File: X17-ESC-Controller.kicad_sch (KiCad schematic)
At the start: 8 parts, among them IC1 STM32F091CCT7, J2 DF11-10DP-2DSA24, J3 DF11-10DP-2DSA24, U1 AZ1117H-ADJ, U2 MAX485CSA+T

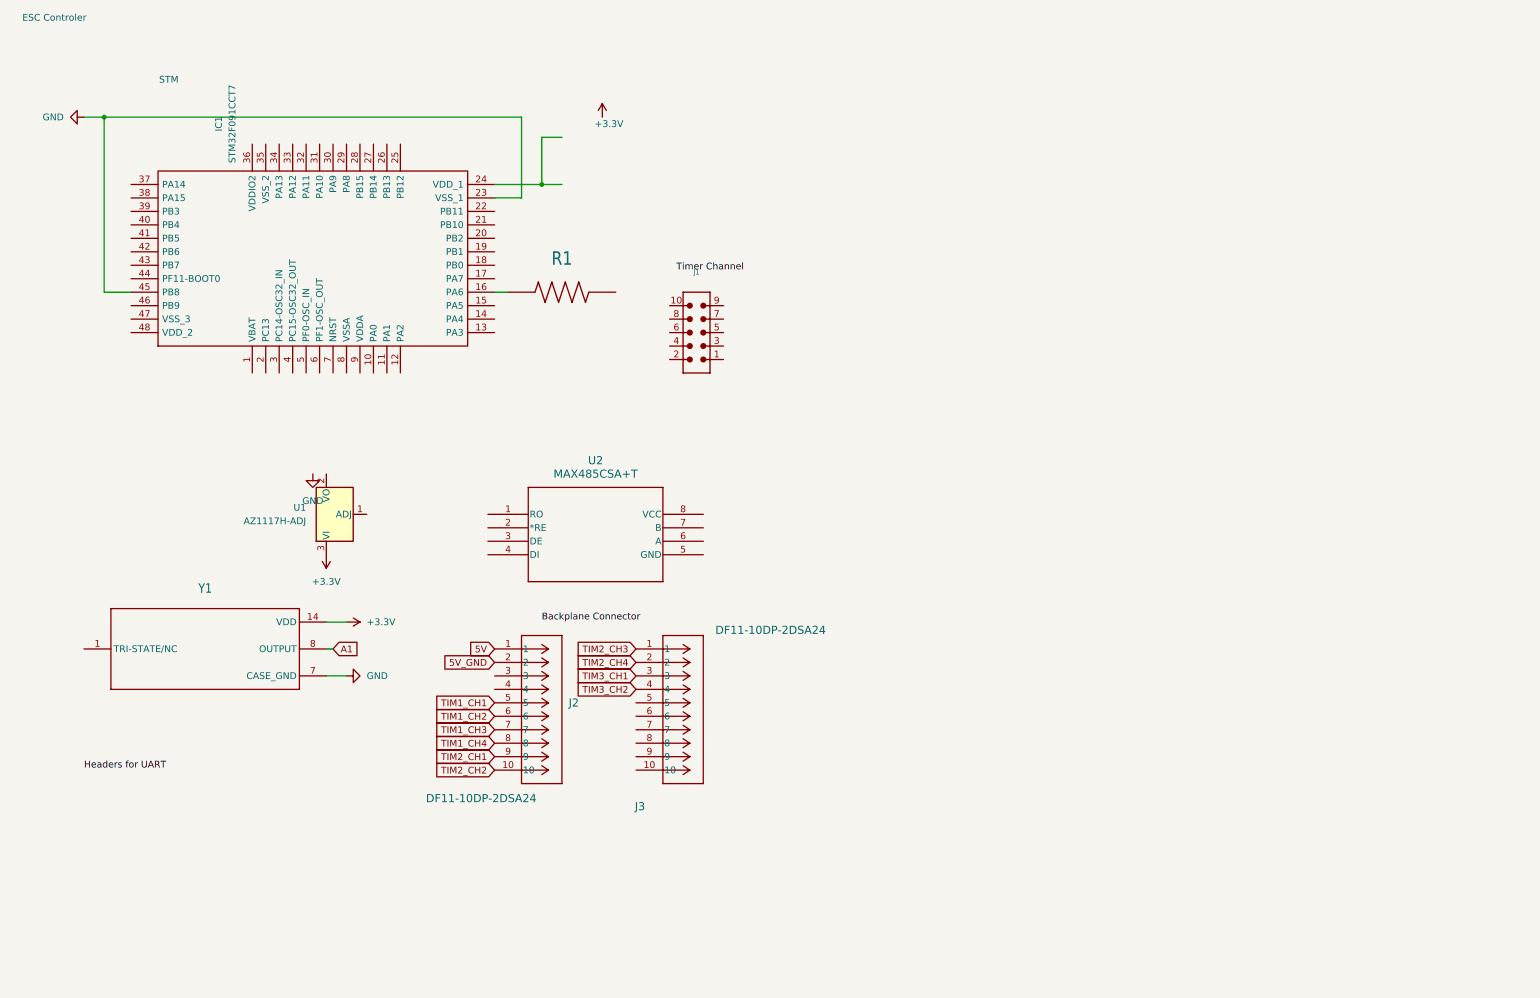
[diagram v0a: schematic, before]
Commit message: X17 ESC Controller Schematic
New updated schematic
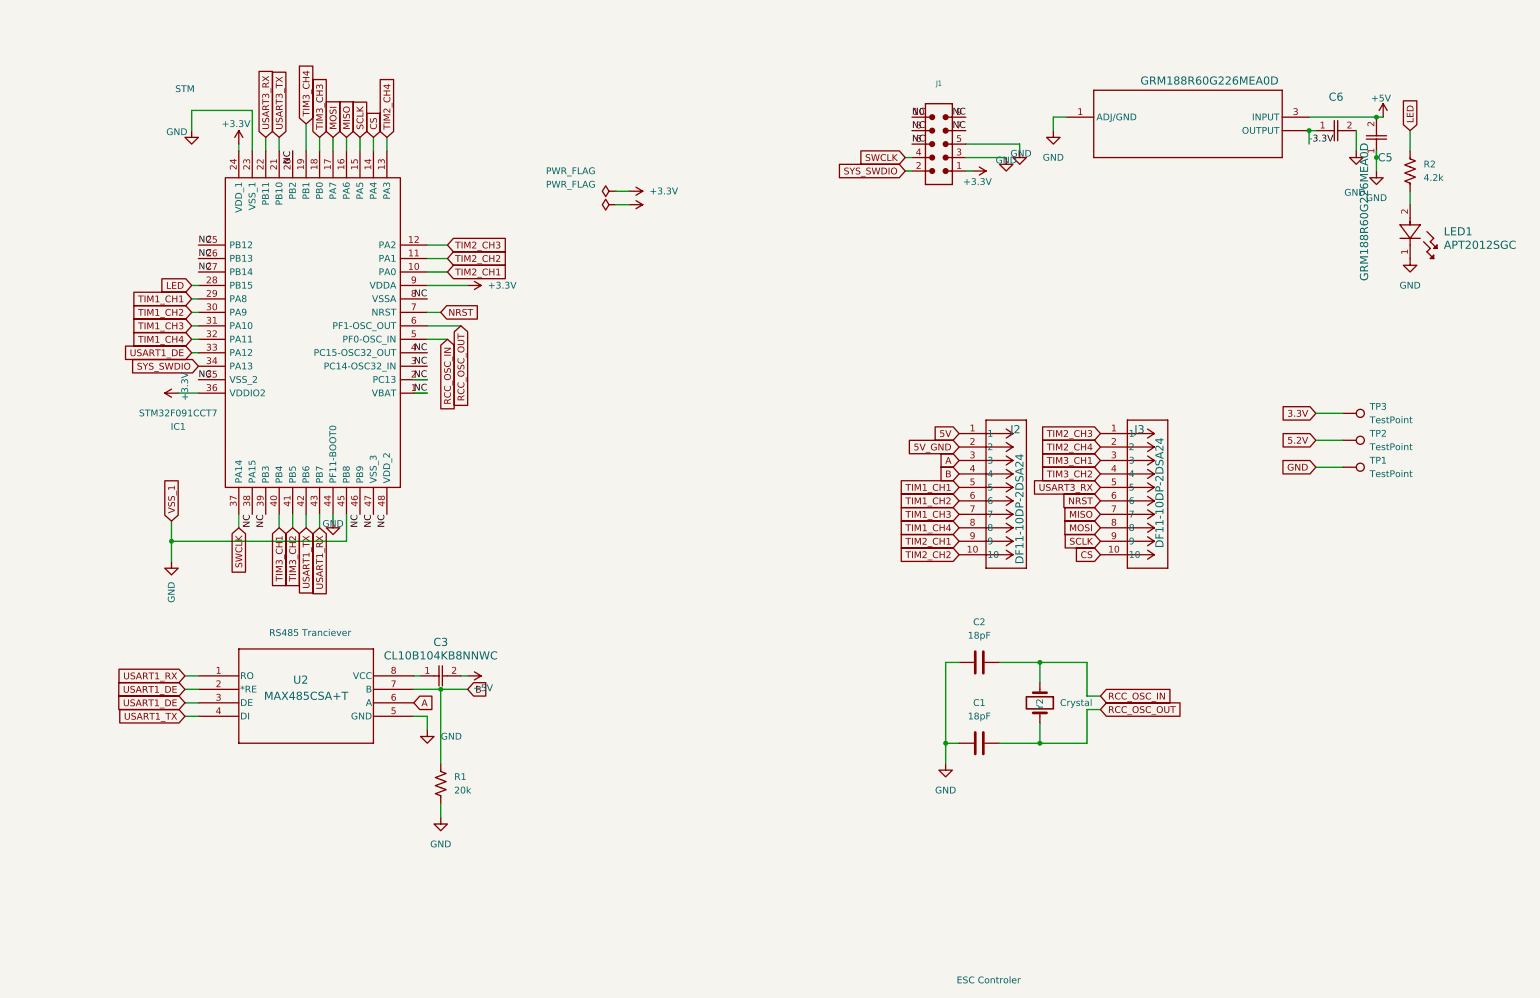
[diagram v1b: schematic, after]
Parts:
- removed R1: ~, CRGCQ0603F1K0:RESC1608X55N, symbol CRGCQ0603F1K0:CRGCQ0603F1K0
- removed U1: AZ1117H-ADJ, Package_TO_SOT_SMD:SOT-223-3_TabPin2, symbol Regulator_Linear:AZ1117H-ADJ
- removed Y1: ~, ACO-8.000MHZ-EK:XTAL_ACO-8.000MHZ-EK, symbol ACO-8.000MHZ-EK:ACO-8.000MHZ-EK
- added C1, C2: 18pF, symbol Device:C
- added C3: CL10B104KB8NNWC, CAP_CL10_SAM, symbol 2024-10-16_23-50-01:CL10B104KB8NNWC
- added C5, C6: GRM188R60G226MEA0D, G-188_MUR, symbol 2024-10-30_23-26-29:GRM188R60G226MEA0D
- added LED1: APT2012SGC, LED_APT2012SGC_KNB, symbol 2024-10-19_19-01-08:APT2012SGC
- added R1: 20k, symbol Device:R_US
- added R2: 4.2k, symbol Device:R_US
- added TP1, TP2, TP3: TestPoint, symbol Connector:TestPoint
- added U3: ~, X16-ESC-Controller:SOT223_AZ1117I_6P5X3P5_DIO, symbol X16-ESC-Controller:AZ1117IH-3.3TRG1
- added Y2: Crystal, symbol Device:Crystal
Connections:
- net +3.3V: now also IC1.24 (VDD_1), IC1.36 (VDDIO2), IC1.9 (VDDA), J1.1
- net GND: now also IC1.44 (PF11-BOOT0), J1.3, J1.5, U2.5 (GND), C1.2, C2.2, C5.1, C6.2, LED1.1, R1.2, TP1.1, U3.1 (ADJ/GND)
- net TIM1_CH1: now also IC1.29 (PA8)
- net TIM1_CH2: now also IC1.30 (PA9)
- net TIM1_CH3: now also IC1.31 (PA10)
- net TIM1_CH4: now also IC1.32 (PA11)
- net TIM2_CH1: now also IC1.10 (PA0)
- net TIM2_CH2: now also IC1.11 (PA1)
- net TIM2_CH3: now also IC1.12 (PA2)
- net TIM2_CH4: now also IC1.13 (PA3)
- net TIM3_CH1: now also IC1.40 (PB4)
- net TIM3_CH2: now also IC1.41 (PB5)
- net MISO: now reaches IC1.16 (PA6)
- net MISO: now also J3.7
- net A: now reaches J2.3
- net A: now also U2.6 (A)
- net B: now reaches J2.4
- net B: now also U2.7 (B), R1.1
- net USART1_RX: now reaches U2.1 (RO)
- net USART1_RX: now also IC1.43 (PB7)
- net USART1_DE: now reaches U2.2 (*RE)
- net USART1_DE: now also IC1.33 (PA12), U2.3 (DE)
- net USART1_TX: now reaches U2.4 (DI)
- net USART1_TX: now also IC1.42 (PB6)
- net at U2.8 (VCC): now also C3.1
- net NC: now reaches IC1.1 (VBAT)
- net NC: now also IC1.2 (PC13), IC1.20 (PB2), IC1.25 (PB12), IC1.26 (PB13), IC1.27 (PB14), IC1.3 (PC14-OSC32_IN), IC1.35 (VSS_2), IC1.38 (PA15), IC1.39 (PB3), IC1.4 (PC15-OSC32_OUT), IC1.46 (PB9), IC1.47 (VSS_3), IC1.48 (VDD_2), IC1.8 (VSSA), J1.10, J1.6, J1.7, J1.8, J1.9
- net CS: now reaches IC1.14 (PA4)
- net CS: now also J3.10
- net SCLK: now reaches IC1.15 (PA5)
- net SCLK: now also J3.9
- net MOSI: now reaches IC1.17 (PA7)
- net MOSI: now also J3.8
- net TIM3_CH3: now reaches IC1.18 (PB0)
- net TIM3_CH4: now reaches IC1.19 (PB1)
- net USART3_TX: now reaches IC1.21 (PB10)
- net USART3_RX: now reaches IC1.22 (PB11)
- net USART3_RX: now also J3.5
- net LED: now reaches IC1.28 (PB15)
- net LED: now also R2.1
- net SYS_SWDIO: now reaches IC1.34 (PA13)
- net SYS_SWDIO: now also J1.2
- net SWCLK: now reaches IC1.37 (PA14)
- net SWCLK: now also J1.4
- net RCC_OSC_IN: now reaches IC1.5 (PF0-OSC_IN)
- net RCC_OSC_IN: now also C2.1, Y2.1
- net RCC_OSC_OUT: now reaches IC1.6 (PF1-OSC_OUT)
- net RCC_OSC_OUT: now also C1.1, Y2.2
- net NRST: now reaches IC1.7 (NRST)
- net NRST: now also J3.6
- new net: LED1.2, R2.2
- new net +5V: C3.2, C5.2, U3.3 (INPUT)
- new net -3.3V: C6.1, U3.2 (OUTPUT), U3.4 (OUTPUT)
- new net 3.3V: TP3.1
- new net 5.2V: TP2.1
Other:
- note added: "RS485 Tranciever"
- moved on the sheet: IC1, J1, J2, J3, U2
